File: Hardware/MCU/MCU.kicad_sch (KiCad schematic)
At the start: 34 parts, among them J1 spi0, J10 i2c1, J11 1778612, J12 i2c0, J2 i2s, J3 1778612, J5 1778612, J6 sp1, J7 sp2, J8 USB_C_Receptacle_USB2.0_16P, J9 1778612, SW1 SW_Push, SW2 SW_Push, U1 ESP32-S3-WROOM-1, U2 USBLC6-2P6

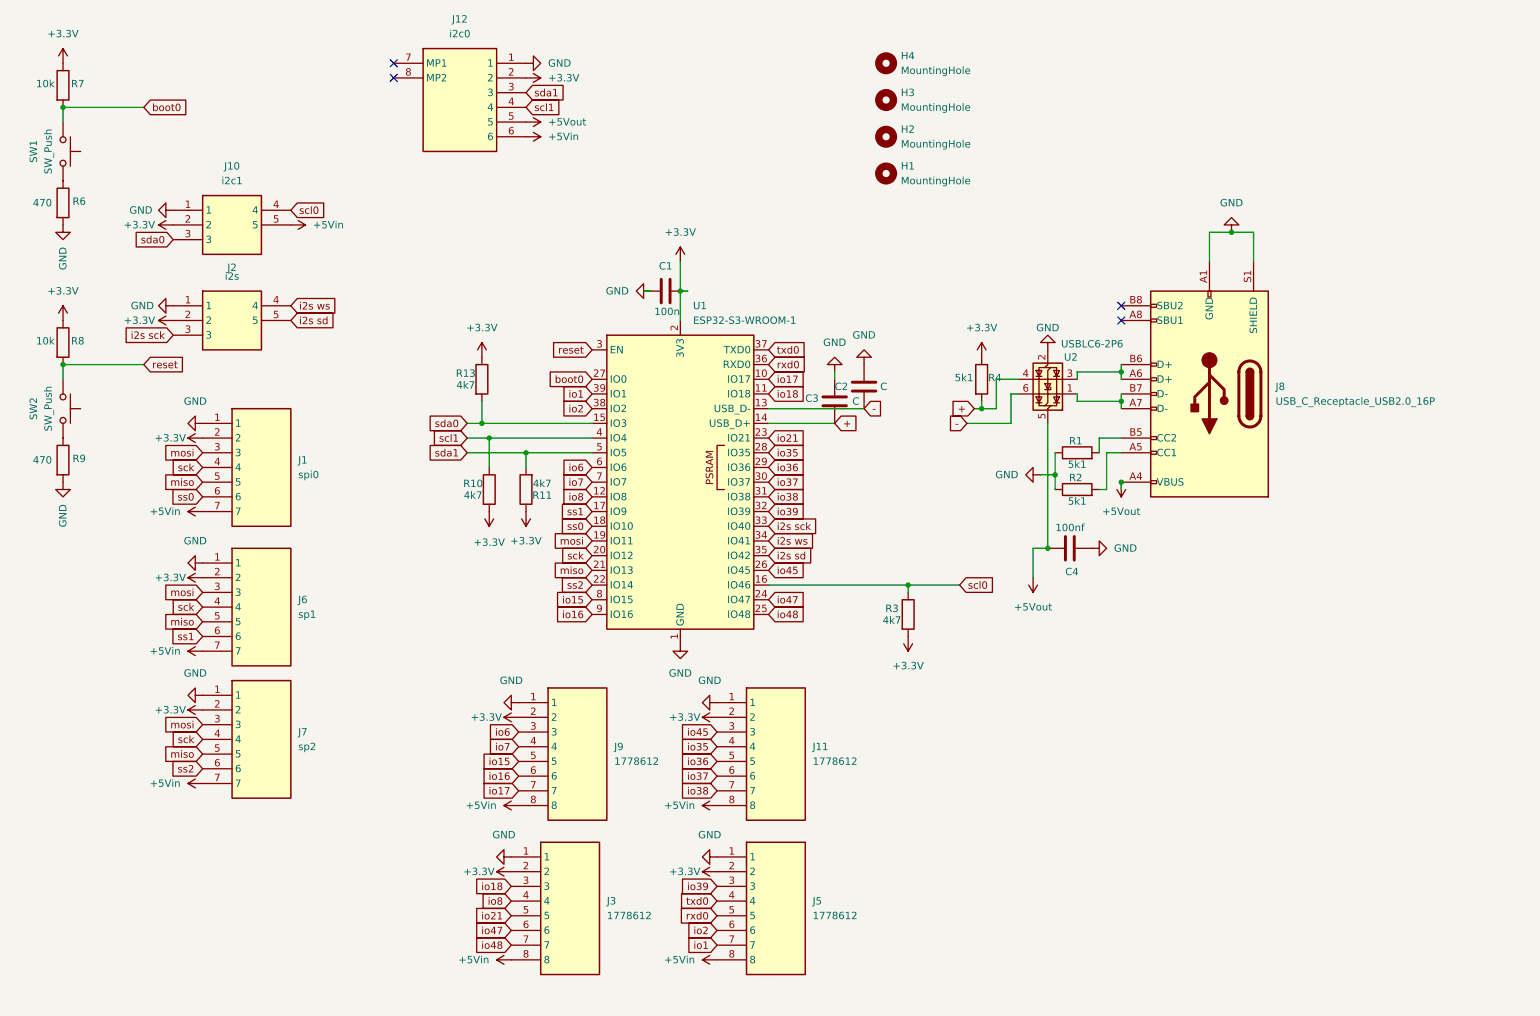
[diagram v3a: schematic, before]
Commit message: schematische tekening geordend
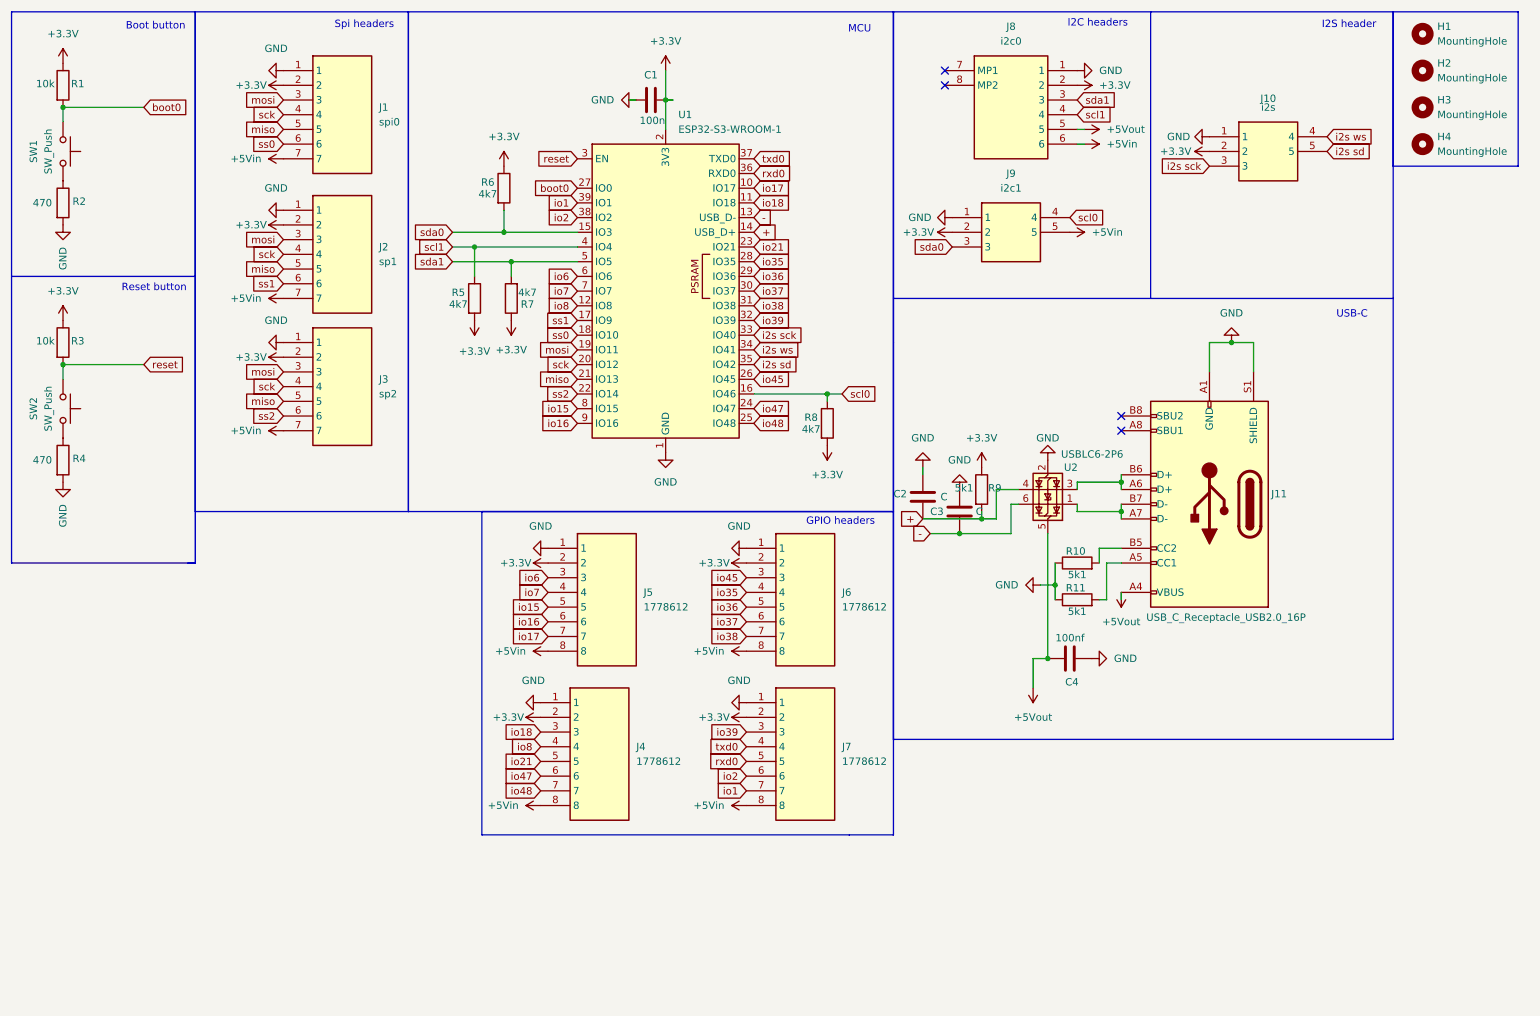
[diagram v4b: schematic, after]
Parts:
- renumbered H4 to H1, H3 to H2, H2 to H3, H1 to H4, J2 to J10, J8 to J11, J6 to J2, J7 to J3, J3 to J4, J9 to J5, J11 to J6, J5 to J7, J12 to J8, J10 to J9, R7 to R1, R1 to R10, R2 to R11, R6 to R2, R8 to R3, R9 to R4, R10 to R5, R13 to R6, R11 to R7, R3 to R8, R4 to R9
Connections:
- net +: now also C2.2; no longer C3.2
- net -: now also C3.2; no longer C2.2
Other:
- note added: "Boot button"
- note added: "GPIO headers"
- note added: "I2C headers"
- note added: "I2S header"
- note added: "MCU"
- note added: "Reset button"
- note added: "Spi headers"
- note added: "USB-C"
- moved on the sheet: C1, C4, H1, H2, H3, H4, J1, J10, J11, J2, J3, J4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

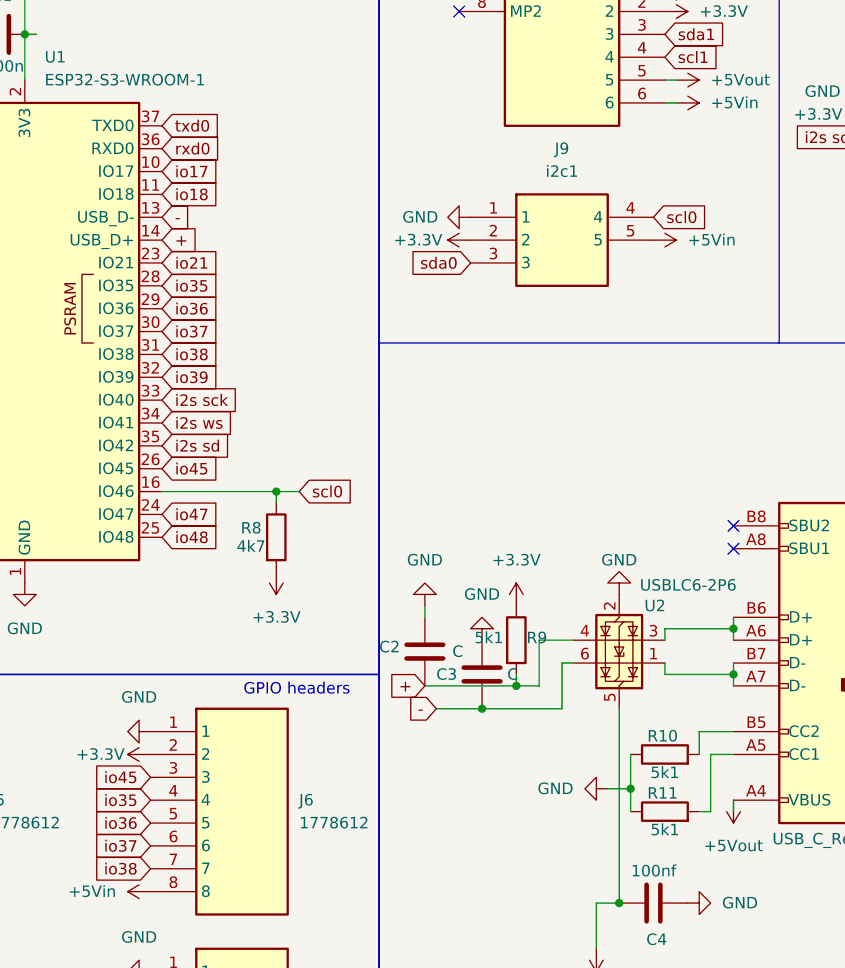
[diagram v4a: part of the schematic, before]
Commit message: added usb weerstanden
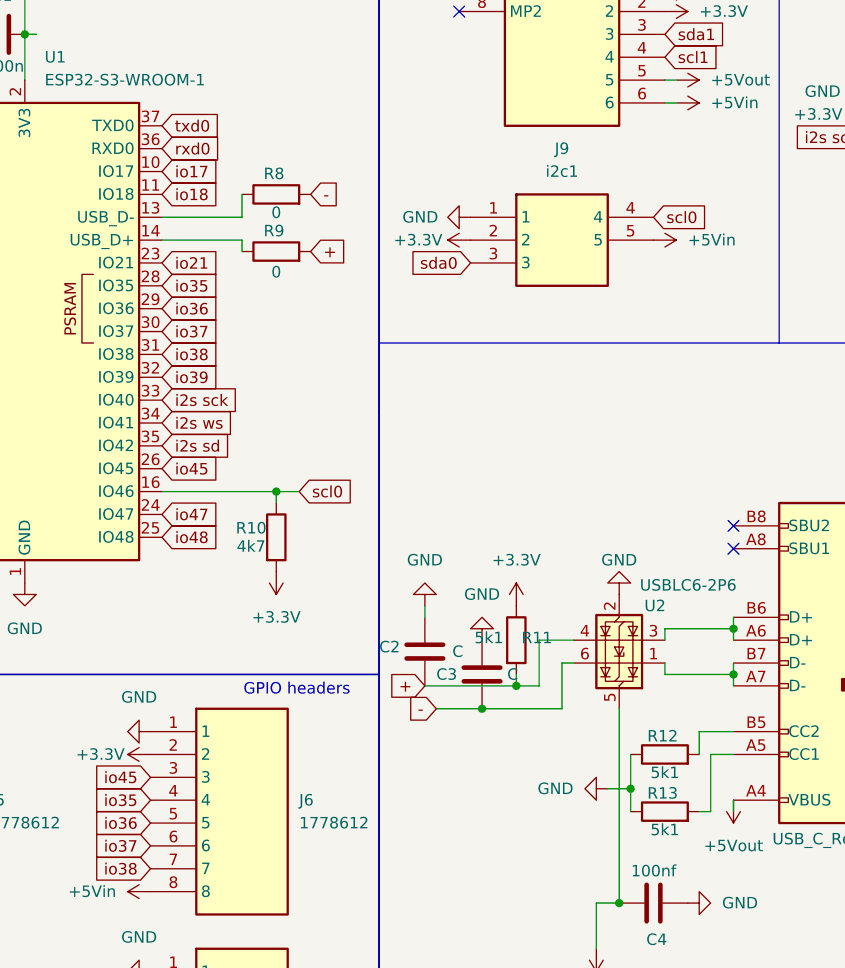
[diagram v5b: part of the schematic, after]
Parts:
- added R8, R9: 0, Resistor_SMD:R_1206_3216Metric_Pad1.30x1.75mm_HandSolder, symbol Device:R
- renumbered R8 to R10, R9 to R11, R10 to R12, R11 to R13
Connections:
- net +: now also R9.2; no longer U1.14 (USB_D+)
- net -: now also R8.2; no longer U1.13 (USB_D-)
- new net: R9.1, U1.14 (USB_D+)
- new net: R8.1, U1.13 (USB_D-)
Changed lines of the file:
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@@
 	(wire
 		(pts
+			(xy 143.51 52.07) (xy 152.4 52.07)
+		)
+		(stroke
+			(width 0)
+			(type default)
+		)
+	)
+	(wire
+		(pts
 			(xy 182.88 101.6) (xy 185.42 101.6)
 		)
@@
 	(wire
 		(pts
+			(xy 143.51 49.53) (xy 152.4 49.53)
+		)
+		(stroke
+			(width 0)
+			(type default)
+		)
+	)
+	(wire
+		(pts
 			(xy 207.01 93.98) (xy 207.01 95.25)
 		)
@@
 		)
 	)
+	(wire
+		(pts
+			(xy 152.4 49.53) (xy 152.4 46.99)
+		)
+		(stroke
+			(width 0)
+			(type default)
+		)
+	)
 	(polyline
 		(pts
@@
 		)
 	)
+	(wire
+		(pts
+			(xy 152.4 52.07) (xy 152.4 53.34)
+		)
+		(stroke
+			(width 0)
+			(type default)
+		)
+	)
 	(polyline
 		(pts
@@
 		)
 	)
+	(global_label "+"
+		(shape input)
+		(at 160.02 53.34 0)
+		(fields_autoplaced yes)
+		(effects
+			(font
+				(size 1.27 1.27)
+			)
+			(justify left)
+		)
+		(property "Intersheetrefs" "${INTERSHEET_REFS}"
+			(at 164.5776 53.34 0)
+			(effects
+				(font
+					(size 1.27 1.27)
+				)
+				(justify left)
+				(hide yes)
+			)
+		)
+	)
 	(global_label "io21"
 		(shape input)
@@
 		)
 	)
+	(global_label "-"
+		(shape input)
+		(at 160.02 46.99 0)
+		(fields_autoplaced yes)
+		(effects
+			(font
+				(size 1.27 1.27)
+			)
+			(justify left)
+		)
+		(property "Intersheetrefs" "${INTERSHEET_REFS}"
+			(at 164.5776 46.99 0)
+			(effects
+				(font
+					(size 1.27 1.27)
+				)
+				(justify left)
+				(hide yes)
+			)
+		)
+	)
 	(global_label "ss2"
 		(shape input)
@@
 		)
 	)
-	(global_label "+"
-		(shape input)
-		(at 143.51 52.07 0)
-		(fields_autoplaced yes)
-		(effects
-			(font
-				(size 1.27 1.27)
-			)
-			(justify left)
-		)
-		(property "Intersheetrefs" "${INTERSHEET_REFS}"
-			(at 148.0676 52.07 0)
-			(effects
-				(font
-					(size 1.27 1.27)
-				)
-				(justify left)
-				(hide yes)
-			)
-		)
-	)
 	(global_label "io1"
 		(shape input)
@@
 		)
 	)
-	(global_label "-"
-		(shape input)
-		(at 143.51 49.53 0)
-		(fields_autoplaced yes)
-		(effects
-			(font
-				(size 1.27 1.27)
-			)
-			(justify left)
-		)
-		(property "Intersheetrefs" "${INTERSHEET_REFS}"
-			(at 148.0676 49.53 0)
-			(effects
-				(font
-					(size 1.27 1.27)
-				)
-				(justify left)
-				(hide yes)
-			)
-		)
-	)
 	(global_label "scl0"
 		(shape input)
@@
 		(on_board yes)
 		(dnp no)
-		(property "Reference" "R11"
+		(property "Reference" "R13"
 			(at 199.136 113.538 90)
 			(effects
@@
 			(project "MCU"
 				(path "/31f46fa8-d9f1-4740-9976-baca520429e4"
-					(reference "R11")
+					(reference "R13")
 					(unit 1)
 				)
@@
 	)
 	(symbol
+		(lib_id "Device:R")
+		(at 156.21 53.34 90)
+		(unit 1)
+		(exclude_from_sim no)
+		(in_bom yes)
+		(on_board yes)
+		(dnp no)
+		(property "Reference" "R9"
+			(at 155.956 51.054 90)
+			(effects
+				(font
+					(size 1.27 1.27)
+				)
+			)
+		)
+		(property "Value" "0"
+			(at 156.21 55.626 90)
+			(effects
+				(font
+					(size 1.27 1.27)
+				)
+			)
+		)
+		(property "Footprint" "Resistor_SMD:R_1206_3216Metric_Pad1.30x1.75mm_HandSolder"
+			(at 156.21 55.118 90)
+			(effects
+				(font
+					(size 1.27 1.27)
+				)
+				(hide yes)
+			)
+		)
+		(property "Datasheet" "~"
+			(at 156.21 53.34 0)
+			(effects
+				(font
+					(size 1.27 1.27)
+				)
+				(hide yes)
+			)
+		)
+		(property "Description" "Resistor"
+			(at 156.21 53.34 0)
+			(effects
+				(font
+					(size 1.27 1.27)
+				)
+				(hide yes)
+			)
+		)
+		(pin "1"
+		)
+		(pin "2"
+		)
+		(instances
+			(project "MCU"
+				(path "/31f46fa8-d9f1-4740-9976-baca520429e4"
+					(reference "R9")
+					(unit 1)
+				)
+			)
+		)
+	)
+	(symbol
 		(lib_id "power:+5V")
 		(at 106.68 151.13 90)
@@
 		(on_board yes)
 		(dnp no)
-		(property "Reference" "R8"
+		(property "Reference" "R10"
 			(at 153.416 84.074 0)
 			(effects
@@
 			(project "MCU"
 				(path "/31f46fa8-d9f1-4740-9976-baca520429e4"
-					(reference "R8")
+					(reference "R10")
 					(unit 1)
 				)
@@
 		(on_board yes)
 		(dnp no)
-		(property "Reference" "R10"
+		(property "Reference" "R12"
 			(at 199.136 107.188 90)
 			(effects
@@
 			(project "MCU"
 				(path "/31f46fa8-d9f1-4740-9976-baca520429e4"
-					(reference "R10")
+					(reference "R12")
 					(unit 1)
 				)
@@
 	)
 	(symbol
+		(lib_id "Device:R")
+		(at 156.21 46.99 90)
+		(unit 1)
+		(exclude_from_sim no)
+		(in_bom yes)
+		(on_board yes)
+		(dnp no)
+		(property "Reference" "R8"
+			(at 155.956 44.704 90)
+			(effects
+				(font
+					(size 1.27 1.27)
+				)
+			)
+		)
+		(property "Value" "0"
+			(at 156.21 49.022 90)
+			(effects
+				(font
+					(size 1.27 1.27)
+				)
+			)
+		)
+		(property "Footprint" "Resistor_SMD:R_1206_3216Metric_Pad1.30x1.75mm_HandSolder"
+			(at 156.21 48.768 90)
+			(effects
+				(font
+					(size 1.27 1.27)
+				)
+				(hide yes)
+			)
+		)
+		(property "Datasheet" "~"
+			(at 156.21 46.99 0)
+			(effects
+				(font
+					(size 1.27 1.27)
+				)
+				(hide yes)
+			)
+		)
+		(property "Description" "Resistor"
+			(at 156.21 46.99 0)
+			(effects
+				(font
+					(size 1.27 1.27)
+				)
+				(hide yes)
+			)
+		)
+		(pin "1"
+		)
+		(pin "2"
+		)
+		(instances
+			(project "MCU"
+				(path "/31f46fa8-d9f1-4740-9976-baca520429e4"
+					(reference "R8")
+					(unit 1)
+				)
+			)
+		)
+	)
+	(symbol
 		(lib_id "power:+3.3V")
 		(at 199.39 26.67 270)
@@
 		(on_board yes)
 		(dnp no)
-		(property "Reference" "R9"
+		(property "Reference" "R11"
 			(at 185.166 96.266 0)
 			(effects
@@
 			(project "MCU"
 				(path "/31f46fa8-d9f1-4740-9976-baca520429e4"
-					(reference "R9")
+					(reference "R11")
 					(unit 1)
 				)

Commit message: edited footprint buttons
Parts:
- SW1, SW2: footprint Capacitor_SMD:C_1206_3216Metric_Pad1.33x1.80mm_HandSolder -> Button_Switch_SMD:SW_SPST_CK_RS282G05A3
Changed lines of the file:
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@@
 			)
 		)
-		(property "Footprint" "Capacitor_SMD:C_1206_3216Metric_Pad1.33x1.80mm_HandSolder"
+		(property "Footprint" "Button_Switch_SMD:SW_SPST_CK_RS282G05A3"
 			(at 29.21 38.1 0)
 			(effects
@@
 			)
 		)
-		(property "Footprint" "Capacitor_SMD:C_1206_3216Metric_Pad1.33x1.80mm_HandSolder"
+		(property "Footprint" "Button_Switch_SMD:SW_SPST_CK_RS282G05A3"
 			(at 29.21 82.55 0)
 			(effects
